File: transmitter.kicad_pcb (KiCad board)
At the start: 6 copper layers, 0 parts

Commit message: added schematics and pcb, configure project
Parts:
- added C1: 100nF, 0_capacitors:C_0402_1005Metric, F.Cu at (148.1, 165.1)
- added C10: 100nF, 0_capacitors:C_0402_1005Metric, F.Cu at (108.5, 208.5)
- added C11: 100nF, 0_capacitors:C_0402_1005Metric, F.Cu at (108.5, 210.5)
- added C12: 4.7uF, 0_capacitors:C_0805_2012Metric, F.Cu at (104.9, 209.1)
- added C13: 4.7uF, 0_capacitors:C_0805_2012Metric, F.Cu at (104.9, 212.1)
- added C2: 100nF, 0_capacitors:C_0402_1005Metric, F.Cu at (148.1, 167.1)
- added C3: 100nF, 0_capacitors:C_0402_1005Metric, F.Cu at (148.1, 169.1)
- added C4: 100nF, 0_capacitors:C_0402_1005Metric, F.Cu at (148.1, 171.0)
- added C5: 100nF, 0_capacitors:C_0402_1005Metric, F.Cu at (148.1, 173.0)
- added C6: 100nF, 0_capacitors:C_0402_1005Metric, F.Cu at (148.1, 175.0)
- added C7: 100nF, 0_capacitors:C_0402_1005Metric, F.Cu at (148.1, 176.9)
- added C8: 100nF, 0_capacitors:C_0402_1005Metric, F.Cu at (155.9, 191.8)
- added C9: 100nF, 0_capacitors:C_0402_1005Metric, F.Cu at (141.1, 193.0)
- added CARD1: ~, 0_connectors:TF-SMD_TF-PUSH, F.Cu at (160.4, 170.7)
- added IC1: W9864G6KH-6, 0_integrated_circuits:SOP80P1176X120-54N, F.Cu at (139.5, 176.1)
- added IC2: TPS61165DBVR, 0_integrated_circuits:SOT95P280X145-6N, F.Cu at (135.0, 192.3)
- added J1: AFC01-S40FCA-00, 0_connectors:AFC01S40FCA00, F.Cu at (76.8, 203.2)
- added J2: AFC07-S10ECC-00, 0_connectors:AFC07S10ECC00, F.Cu at (108.0, 202.9)
- added R1: 10kΩ, 0_resistors:R_0402_1005Metric, F.Cu at (153.0, 184.1)
- added R2: 10kΩ, 0_resistors:R_0402_1005Metric, F.Cu at (153.0, 186.0)
- added R3: 10kΩ, 0_resistors:R_0402_1005Metric, F.Cu at (153.0, 188.0)
- added R4: 10kΩ, 0_resistors:R_0402_1005Metric, F.Cu at (153.0, 190.0)
- added R5: 0Ω, 0_resistors:R_0402_1005Metric, F.Cu at (153.0, 192.0)
- added R6: 0Ω, 0_resistors:R_0402_1005Metric, F.Cu at (153.0, 194.0)
- added R7: 10kΩ, 0_resistors:R_0402_1005Metric, F.Cu at (141.1, 191.0)
- added R8: 10kΩ, 0_resistors:R_0402_1005Metric, F.Cu at (111.4, 208.5)
- added U1: STM32H743ZIT6TR, 0_integrated_circuits:LQFP-144_1_STM, F.Cu at (120.7, 151.3)
- added U2: CAT24C256, 0_integrated_circuits:SOIC-8_5.3x6.2mm_P1.27mm, F.Cu at (159.7, 186.9)
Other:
- board outline added: 200 x 200 mm
- copper layers 6 -> 2
- rule pad_to_mask_clearance: 0.05 -> 0
- board text removed: "??? ??? ???"
- board text removed: "??? ??? ??? ??? ??? (slot) ??? ??? ??? ??? ???"
- board text removed: "???mm"
- board text removed: "???mm (?oz)"
- board text removed: "???mm ???mm ???mm ???mm ???mm ???mm ???mm ???mm ???mm ???mm"
- board text removed: "ASSEMBLY NOTES (UNLESS OTHERWISE SPECIFIED) 1) DO NOT POPULATE PARTS ARE MARKED WITH A RED CROSS. 2) DO NOT POPULATE PARTS ARE NOT PRESENT IN THE BOM. 3) IF CONFLICTING INFORMATION IS FOUND BETWEEN THE ASSEMBLY FILE AND BOM, BOM SHOULD BE USED AS THE MAIN SOURCE."
- board text removed: "All dimensions are in millimeters unless otherwise specified."
- board text removed: "B.Mask"
- board text removed: "B.Paste"
- board text removed: "B.Silkscreen"
- board text removed: "Back Side"
- board text removed: "Bottom Assembly (Scale 1:1)"
- board text removed: "Bottom Fabrication (Scale 1:1)"
- board text removed: "Bottom Test Points (Scale 1:1)"
- board text removed: "Bottom View"
- board text removed: "Components"
- board text removed: "Copper"
- board text removed: "Core"
- board text removed: "Count"
- board text removed: "Dielectric"
- board text removed: "Dielectric Material"
- board text removed: "Drill Drawing (Top View) (Scale 1:1)"
- board text removed: "F.Mask"
- board text removed: "F.Paste"
- board text removed: "F.Silkscreen"
- board text removed: "FABRICATION NOTES (UNLESS OTHERWISE SPECIFIED) 1) OUTLINE DEFINED IN SEPARATE GERBER FILE WITH {dblquote}Edge_Cuts.GBR{dblquote} SUFFIX. DIMENSIONS OF CIRCUMSIZED RECTANGLE SHOWN ON THIS DWG FOR REF ONLY. 2) SEE SEPARATE DRILL FILES WITH {dblquote}.DRL{dblquote} SUFFIX FOR HOLE LOCATIONS. SELECTED HOLE LOCATIONS SHOWN ON THIS DWG FOR REF ONLY. 3) IMPEDANCE CONTROL REQUIRED. Microstrip 100-Ohm Dif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"
- board text removed: "FR-4"
- board text removed: "Front Side"
- board text removed: "GBR"
- board text removed: "Gerber"
- board text removed: "Hole Size"
- board text removed: "Internal Plane"
- board text removed: "L1 (Sig, PWR)"
- board text removed: "L2 (GND)"
- board text removed: "L3 (Sig, PWR)"
- board text removed: "L4 (Sig, PWR)"
- board text removed: "L5 (GND)"
- board text removed: "L6 (Sig, PWR)"
- board text removed: "Layer"
- board text removed: "Layer Stack Legend"
- board text removed: "Legend"
- board text removed: "Material"
- board text removed: "Net"
- board text removed: "Note: external layer thicknesses are specified after plating."
- board text removed: "PCB3D_BR_BOARDNAME"
- board text removed: "PCB3D_TL_BOARDNAME"
- board text removed: "Paste Mask"
- board text removed: "Plated"
- board text removed: "Plated Plated Plated Plated Plated Plated Plated Plated Plated Unplated"
- board text removed: "Prepreg"
- board text removed: "Ref."
- board text removed: "Signal"
- board text removed: "Solder Mask"
- board text removed: "Solder Resist"
- board text removed: "Symbol"
- board text removed: "THT SMD Total"
- board text removed: "TP? TP? TP?"
- board text removed: "Thickness"
- board text removed: "Top Assembly (Scale 1:1)"
- board text removed: "Top Fabrication (Scale 1:1)"
- board text removed: "Top Test Points (Scale 1:1)"
- board text removed: "Top View"
- board text removed: "Total"
- board text removed: "Total thickness: 1.62mm"
- board text removed: "Type"
- board text removed: "X"
- board text removed: "X [mm]"
- board text removed: "Y"
- board text removed: "Y [mm]"

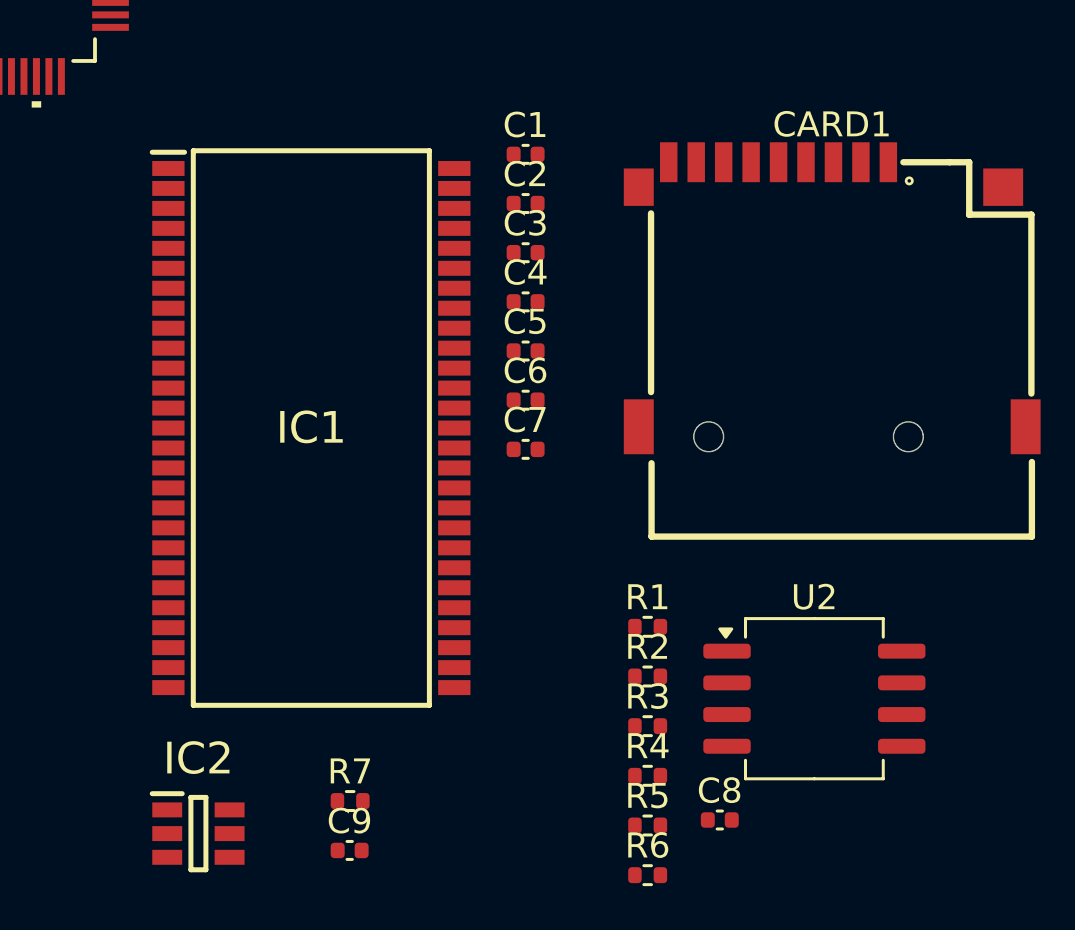
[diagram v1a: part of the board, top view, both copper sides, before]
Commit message: added lcd backlight schematic
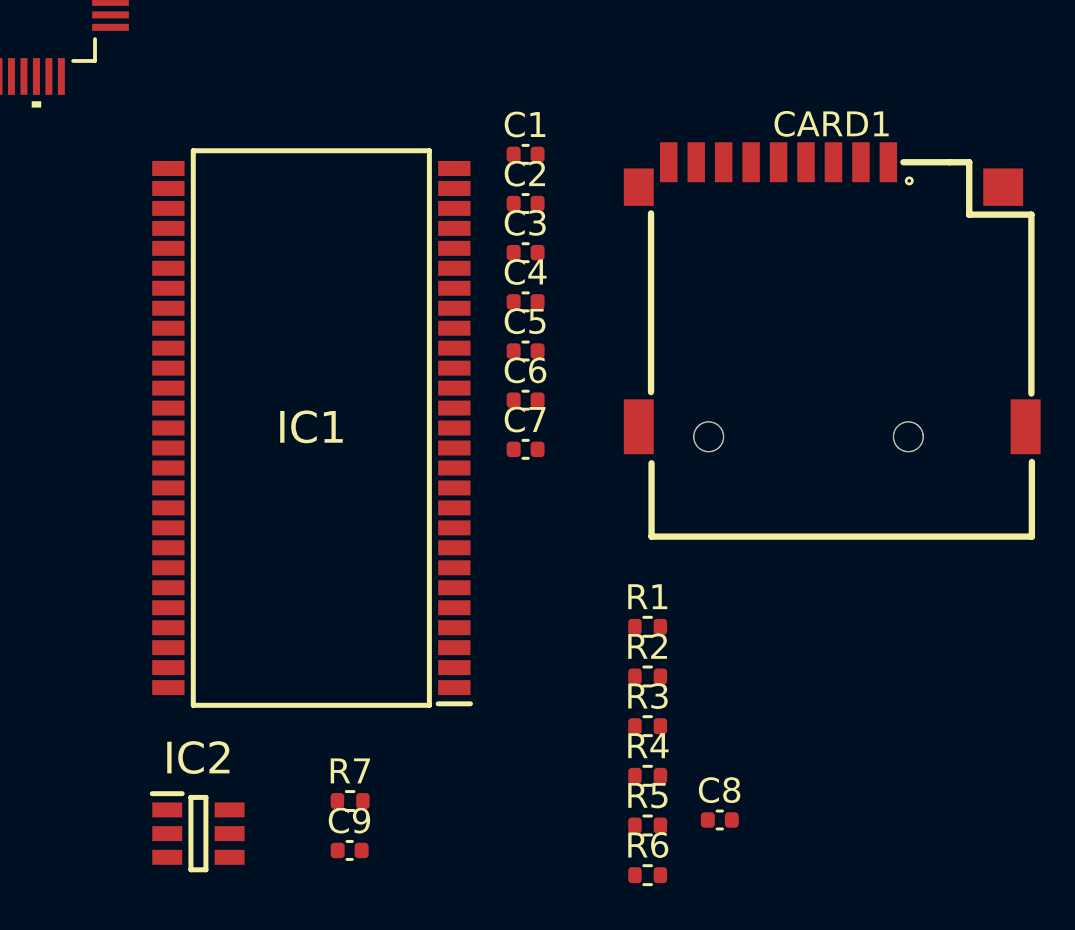
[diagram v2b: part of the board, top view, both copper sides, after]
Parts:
- removed U2: CAT24C256, 0_integrated_circuits:SOIC-8_5.3x6.2mm_P1.27mm
- turned IC1 to 180 degrees

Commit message: update project structure and import to pcb
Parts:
- added BZ1: Buzzer, Buzzer_Beeper:Buzzer_TDK_PS1240P02BT_D12.2mm_H6.5mm, F.Cu at (329.8, 83.2)
- added C14: 4.7uF, 0_capacitors:C_0805_2012Metric, F.Cu at (298.9, 29.1)
- added C15: 100nF, 0_capacitors:C_0402_1005Metric, F.Cu at (302.6, 38.7)
- added C16: 4.7uF, 0_capacitors:C_0805_2012Metric, F.Cu at (298.9, 32.1)
- added C17: 4.7uF, 0_capacitors:C_0805_2012Metric, F.Cu at (298.9, 35.1)
- added C18: 220nF, 0_capacitors:C_0402_1005Metric, F.Cu at (302.6, 40.7)
- added C19: 10uF 16V, 0_capacitors:CP_EIA-3216-18_Kemet-A, F.Cu at (252.9, 48.3)
- added C20: 100nF, 0_capacitors:C_0402_1005Metric, F.Cu at (264.5, 47.7)
- added C21: 4.7uF, 0_capacitors:C_0805_2012Metric, F.Cu at (257.9, 48.2)
- added C22: 100nF, 0_capacitors:C_0402_1005Metric, F.Cu at (148.0, 91.2)
- added C23: 100nF, 0_capacitors:C_0402_1005Metric, F.Cu at (328.6, 105.6)
- added C24: 100nF, 0_capacitors:C_0402_1005Metric, F.Cu at (328.6, 107.5)
- added C25: 100nF, 0_capacitors:C_0402_1005Metric, F.Cu at (328.6, 109.5)
- added C26: 100nF, 0_capacitors:C_0402_1005Metric, F.Cu at (328.6, 111.5)
- added C27: 100nF, 0_capacitors:C_0402_1005Metric, F.Cu at (285.8, 78.9)
- added C28: 100nF, 0_capacitors:C_0402_1005Metric, F.Cu at (285.8, 80.9)
- added C29: 100nF, 0_capacitors:C_0402_1005Metric, F.Cu at (285.8, 82.9)
- added C30: 100nF, 0_capacitors:C_0402_1005Metric, F.Cu at (285.8, 84.8)
- added C31: 100nF, 0_capacitors:C_0402_1005Metric, F.Cu at (285.8, 86.8)
- added C32: 100nF, 0_capacitors:C_0402_1005Metric, F.Cu at (285.8, 88.8)
- added C33: 100nF, 0_capacitors:C_0402_1005Metric, F.Cu at (285.8, 90.7)
- added C34: 100nF, 0_capacitors:C_0402_1005Metric, F.Cu at (285.8, 92.7)
- added C35: 100nF, 0_capacitors:C_0402_1005Metric, F.Cu at (332.4, 35.2)
- added C36: 100nF, 0_capacitors:C_0402_1005Metric, F.Cu at (332.4, 37.1)
- added C37: 4.7uF, 0_capacitors:C_0805_2012Metric, F.Cu at (334.2, 98.1)
- added C38: 100nF, 0_capacitors:C_0402_1005Metric, F.Cu at (341.8, 104.7)
- added C39: 4.7uF, 0_capacitors:C_0805_2012Metric, F.Cu at (334.2, 101.2)
- added C40: 10uF, 0_capacitors:C_0805_2012Metric, F.Cu at (333.4, 65.7)
- added C41: 100nF, 0_capacitors:C_0402_1005Metric, F.Cu at (341.8, 106.7)
- added C42: 10uF, 0_capacitors:C_0805_2012Metric, F.Cu at (334.2, 104.2)
- added C43: 100nF, 0_capacitors:C_0402_1005Metric, F.Cu at (340.0, 65.1)
- added C44: 10uF, 0_capacitors:C_0805_2012Metric, F.Cu at (293.2, 62.5)
- added C45: 10uF, 0_capacitors:C_0805_2012Metric, F.Cu at (293.2, 65.6)
- added C46: 1uF, 0_capacitors:C_0603_1608Metric, F.Cu at (279.3, 68.4)
- added C47: 100nF, 0_capacitors:C_0402_1005Metric, F.Cu at (282.8, 68.1)
- added C48: 100pF, 0_capacitors:C_0603_1608Metric, F.Cu at (279.3, 70.9)
- added C49: 22uF, 0_capacitors:C_0805_2012Metric, F.Cu at (293.2, 68.6)
- added C50: 22uF, 0_capacitors:C_0805_2012Metric, F.Cu at (293.2, 71.6)
- added C51: 10uF 16V, 0_capacitors:CP_EIA-3216-18_Kemet-A, F.Cu at (298.5, 62.6)
- added C52: 10uF 16V, 0_capacitors:CP_EIA-3216-18_Kemet-A, F.Cu at (298.5, 65.8)
- added C53: 100nF, 0_capacitors:C_0402_1005Metric, F.Cu at (282.8, 70.1)
- added C54: 100nF, 0_capacitors:C_0402_1005Metric, F.Cu at (282.8, 72.0)
- added C55: 100nF, 0_capacitors:C_0402_1005Metric, F.Cu at (251.2, 78.6)
- added C56: 100nF, 0_capacitors:C_0402_1005Metric, F.Cu at (251.2, 80.6)
- added C57: 100nF, 0_capacitors:C_0402_1005Metric, F.Cu at (251.2, 82.6)
- added C58: 100nF, 0_capacitors:C_0402_1005Metric, F.Cu at (251.2, 84.5)
- added C59: 100nF, 0_capacitors:C_0402_1005Metric, F.Cu at (251.2, 86.5)
- added C60: 100nF, 0_capacitors:C_0402_1005Metric, F.Cu at (251.2, 88.5)
- added C61: 100nF, 0_capacitors:C_0402_1005Metric, F.Cu at (254.1, 78.6)
- added C62: 100nF, 0_capacitors:C_0402_1005Metric, F.Cu at (254.1, 80.6)
- added C63: 100nF, 0_capacitors:C_0402_1005Metric, F.Cu at (254.1, 82.6)
- added C64: 100nF, 0_capacitors:C_0402_1005Metric, F.Cu at (254.1, 84.5)
- added C65: 100nF, 0_capacitors:C_0402_1005Metric, F.Cu at (254.1, 86.5)
- added C66: 1uF, 0_capacitors:C_0603_1608Metric, F.Cu at (270.4, 85.5)
- added C67: 1uF, 0_capacitors:C_0603_1608Metric, F.Cu at (270.4, 88.0)
- added C68: 1uF, 0_capacitors:C_0603_1608Metric, F.Cu at (270.4, 90.5)
- added C69: 100nF, 0_capacitors:C_0402_1005Metric, F.Cu at (254.1, 88.5)
- added C70: 100nF, 0_capacitors:C_0402_1005Metric, F.Cu at (256.9, 78.6)
- added C71: 4.7uF, 0_capacitors:C_0805_2012Metric, F.Cu at (272.9, 79.2)
- added C72: 2.2uF, 0_capacitors:C_1206_3216Metric, F.Cu at (265.6, 85.9)
- added C73: 2.2uF, 0_capacitors:C_1206_3216Metric, F.Cu at (265.6, 89.2)
- added C74: 100nF, 0_capacitors:C_0402_1005Metric, F.Cu at (256.9, 80.6)
- added C75: 100nF, 0_capacitors:C_0402_1005Metric, F.Cu at (256.9, 82.6)
- added C76: 100nF, 0_capacitors:C_0402_1005Metric, F.Cu at (281.6, 114.2)
- added C77: 100nF, 0_capacitors:C_0402_1005Metric, F.Cu at (281.6, 116.1)
- added C78: 100nF, 0_capacitors:C_0402_1005Metric, F.Cu at (281.6, 118.1)
- added C79: 100nF, 0_capacitors:C_0402_1005Metric, F.Cu at (258.4, 101.4)
- added C80: 100nF, 0_capacitors:C_0402_1005Metric, F.Cu at (258.4, 103.3)
- added C81: 6.8pF, 0_capacitors:C_0402_1005Metric, F.Cu at (258.4, 105.3)
- added C82: 6.8pF, 0_capacitors:C_0402_1005Metric, F.Cu at (258.4, 107.3)
- added C83: 6.8pF, 0_capacitors:C_0402_1005Metric, F.Cu at (258.4, 109.3)
- added C84: 6.8pF, 0_capacitors:C_0402_1005Metric, F.Cu at (258.4, 111.2)
- added C85: 1uF, 0_capacitors:C_0603_1608Metric, F.Cu at (271.1, 109.6)
- added D1: 1N5819WS, 0_diodes:D_SOD-323, F.Cu at (308.6, 39.6)
- added D2: 1N5819WS, 0_diodes:D_SOD-323, F.Cu at (339.7, 79.4)
- added D3: 1N5819WS, 0_diodes:D_SOD-323, F.Cu at (297.6, 74.5)
- added D4: RED, LED_SMD:LED_0603_1608Metric, F.Cu at (314.8, 42.9)
- added D5: WHITE, LED_SMD:LED_0603_1608Metric, F.Cu at (314.8, 45.5)
- added E01-2G4M27D1: DS1023-2*4SF11, 0_modules:PE01-ML01DP5, F.Cu at (121.9, 39.2)
- added IC3: MT25QL128ABA1ESE-0SIT, 0_integrated_circuits:SOIC127P790X216-8L, F.Cu at (148.5, 86.9)
- added IC4: USBLC6-2SC6, 0_integrated_circuits:SOT95P280X145-6N, F.Cu at (328.6, 66.4)
- added J10: ~, Connector_PinHeader_2.54mm:PinHeader_1x02_P2.54mm_Vertical, F.Cu at (266.7, 117.2)
- added J3: B2B-PH-K-S, Connector_JST:JST_PH_B2B-PH-K_1x02_P2.00mm_Vertical, F.Cu at (265.7, 80.4)
- added J4: B2B-PH-K-S, Connector_JST:JST_PH_B2B-PH-K_1x02_P2.00mm_Vertical, F.Cu at (335.0, 119.5)
- added J5: B3B-PH-K-S, Connector_JST:JST_PH_B3B-PH-K_1x03_P2.00mm_Vertical, F.Cu at (335.0, 112.9)
- added J6: USB4085-GF-A, 0_connectors:GCT_USB4085-GF-A_REVB, F.Cu at (49.4, 25.9)
- added J7: Conn_01x05, Connector_JST:JST_PH_B5B-PH-K_1x05_P2.00mm_Vertical, F.Cu at (259.9, 96.6)
- added J8: ~, Connector_PinHeader_2.54mm:PinHeader_1x02_P2.54mm_Vertical, F.Cu at (262.1, 117.2)
- added J9: Conn_02x06_Odd_Even, Connector_PinSocket_2.54mm:PinSocket_2x06_P2.54mm_Vertical, F.Cu at (254.6, 96.2)
- added JP1: NO, Jumper:SolderJumper-2_P1.3mm_Open_TrianglePad1.0x1.5mm, F.Cu at (298.1, 58.2)
- added JP10: NO, Jumper:SolderJumper-2_P1.3mm_Open_TrianglePad1.0x1.5mm, F.Cu at (338.6, 102.0)
- added JP2: NC, Jumper:SolderJumper-2_P1.3mm_Open_TrianglePad1.0x1.5mm, F.Cu at (260.6, 79.4)
- added JP3: NO, Jumper:SolderJumper-2_P1.3mm_Open_TrianglePad1.0x1.5mm, F.Cu at (260.6, 83.0)
- added JP4: NC, Jumper:SolderJumper-2_P1.3mm_Open_TrianglePad1.0x1.5mm, F.Cu at (271.1, 116.7)
- added JP5: NC, Jumper:SolderJumper-2_P1.3mm_Open_TrianglePad1.0x1.5mm, F.Cu at (260.6, 86.5)
- added JP6: NC, Jumper:SolderJumper-2_P1.3mm_Open_TrianglePad1.0x1.5mm, F.Cu at (260.6, 90.1)
- added JP7: SolderJumper_3_Bridged12, Jumper:SolderJumper-3_P2.0mm_Open_TrianglePad1.0x1.5mm_NumberLabels, F.Cu at (330.5, 90.3)
- added JP8: NO, Jumper:SolderJumper-2_P1.3mm_Open_TrianglePad1.0x1.5mm, F.Cu at (271.1, 120.2)
- added JP9: NO, Jumper:SolderJumper-2_P1.3mm_Open_TrianglePad1.0x1.5mm, F.Cu at (338.6, 98.4)
- added L1: 1.33A 10uH, 0_inductors:IND_VLS3012HBX-100M, F.Cu at (308.0, 30.1)
- added L2: GZ2012D601TF, 0_inductors:L_0805_2012Metric, F.Cu at (303.4, 29.0)
- added L3: GZ2012D601TF, 0_inductors:L_0805_2012Metric, F.Cu at (303.4, 31.8)
- added L4: 1.8A 1uH, Inductor_SMD:L_Cenker_CKCS4018, F.Cu at (298.4, 70.2)
- added Q1: AO3400A, Package_TO_SOT_SMD:SOT-23, F.Cu at (288.5, 63.4)
- added Q2: AO3400A, Package_TO_SOT_SMD:SOT-23, F.Cu at (288.5, 68.1)
- added Q3: SI2301CDS-T1-GE3, 0_transistors:SOT-23, F.Cu at (288.5, 72.7)
- added Q4: AO3400A, Package_TO_SOT_SMD:SOT-23, F.Cu at (336.5, 90.9)
- added R10: 10kΩ, 0_resistors:R_0402_1005Metric, F.Cu at (298.2, 39.6)
- added R11: 1Ω, 0_resistors:R_0603_1608Metric, F.Cu at (308.4, 34.4)
- added R12: 2Ω, 0_resistors:R_0603_1608Metric, F.Cu at (308.4, 36.9)
- added R13: 10kΩ, 0_resistors:R_0402_1005Metric, F.Cu at (261.6, 47.7)
- added R14: 10kΩ, 0_resistors:R_0402_1005Metric, F.Cu at (261.6, 49.7)
- added R15: 10kΩ, 0_resistors:R_0402_1005Metric, F.Cu at (145.1, 91.2)
- added R16: 0Ω, 0_resistors:R_0402_1005Metric, F.Cu at (328.6, 97.6)
- added R17: 0Ω, 0_resistors:R_0402_1005Metric, F.Cu at (328.6, 99.6)
- added R18: 0Ω, 0_resistors:R_0402_1005Metric, F.Cu at (328.6, 101.6)
- added R19: 0Ω, 0_resistors:R_0402_1005Metric, F.Cu at (328.6, 103.6)
- added R20: 47kΩ, 0_resistors:R_0402_1005Metric, F.Cu at (285.8, 94.7)
- added R21: 5.1kΩ, 0_resistors:R_0402_1005Metric, F.Cu at (285.8, 96.7)
- added R22: 5.1kΩ, 0_resistors:R_0402_1005Metric, F.Cu at (285.8, 98.7)
- added R23: 47kΩ, 0_resistors:R_0402_1005Metric, F.Cu at (285.8, 100.7)
- added R24: 5.1kΩ, 0_resistors:R_0402_1005Metric, F.Cu at (288.7, 94.7)
- added R25: 47kΩ, 0_resistors:R_0402_1005Metric, F.Cu at (288.7, 96.7)
- added R26: 5.1kΩ, 0_resistors:R_0402_1005Metric, F.Cu at (288.7, 98.7)
- added R27: 47kΩ, 0_resistors:R_0402_1005Metric, F.Cu at (288.7, 100.7)
- added R28: 5.1kΩ, 0_resistors:R_0402_1005Metric, F.Cu at (291.6, 94.7)
- added R29: 47kΩ, 0_resistors:R_0402_1005Metric, F.Cu at (291.6, 96.7)
- added R30: 5.1kΩ, 0_resistors:R_0402_1005Metric, F.Cu at (291.6, 98.7)
- added R31: 47kΩ, 0_resistors:R_0402_1005Metric, F.Cu at (291.6, 100.7)
- added R32: 5.1kΩ, 0_resistors:R_0402_1005Metric, F.Cu at (294.5, 94.7)
- added R33: 47kΩ, 0_resistors:R_0402_1005Metric, F.Cu at (294.5, 96.7)
- added R34: 5.1kΩ, 0_resistors:R_0402_1005Metric, F.Cu at (294.5, 98.7)
- added R35: 47kΩ, 0_resistors:R_0402_1005Metric, F.Cu at (294.5, 100.7)
- added R36: 5.1kΩ, 0_resistors:R_0402_1005Metric, F.Cu at (329.5, 28.6)
- added R37: 47kΩ, 0_resistors:R_0402_1005Metric, F.Cu at (329.5, 30.6)
- added R38: 5.1kΩ, 0_resistors:R_0402_1005Metric, F.Cu at (329.5, 32.6)
- added R39: 47kΩ, 0_resistors:R_0402_1005Metric, F.Cu at (329.5, 34.6)
- added R40: 47kΩ, 0_resistors:R_0402_1005Metric, F.Cu at (322.5, 53.7)
- added R41: 47kΩ, 0_resistors:R_0402_1005Metric, F.Cu at (322.5, 55.7)
- added R42: 47kΩ, 0_resistors:R_0402_1005Metric, F.Cu at (322.5, 57.7)
- added R43: 47kΩ, 0_resistors:R_0402_1005Metric, F.Cu at (322.5, 59.7)
- added R44: 47kΩ, 0_resistors:R_0402_1005Metric, F.Cu at (322.5, 61.7)
- added R45: 0Ω, 0_resistors:R_0402_1005Metric, F.Cu at (322.5, 63.7)
- added R46: 47kΩ, 0_resistors:R_0402_1005Metric, F.Cu at (322.5, 65.7)
- added R47: 10kΩ, 0_resistors:R_0402_1005Metric, F.Cu at (342.3, 97.6)
- added R48: 10kΩ, 0_resistors:R_0402_1005Metric, F.Cu at (342.3, 99.6)
- added R49: 300kΩ, 0_resistors:R_0603_1608Metric, F.Cu at (334.0, 106.9)
- added R50: 0Ω, 0_resistors:R_0402_1005Metric, F.Cu at (342.3, 101.6)
- added R51: 5.1kΩ, 0_resistors:R_0402_1005Metric, F.Cu at (337.1, 65.1)
- added R52: 5.1kΩ, 0_resistors:R_0402_1005Metric, F.Cu at (337.1, 67.1)
- added R53: 100kΩ, 0_resistors:R_0402_1005Metric, F.Cu at (278.8, 53.7)
- added R54: 0Ω, 0_resistors:R_0402_1005Metric, F.Cu at (278.8, 55.7)
- added R55: 0Ω, 0_resistors:R_0402_1005Metric, F.Cu at (278.8, 57.7)
- added R56: 47kΩ, 0_resistors:R_0402_1005Metric, F.Cu at (278.8, 59.7)
- added R57: 10kΩ, 0_resistors:R_0402_1005Metric, F.Cu at (278.8, 61.7)
- added R58: 0Ω, 0_resistors:R_0402_1005Metric, F.Cu at (281.7, 53.7)
- added R59: 0Ω, 0_resistors:R_0402_1005Metric, F.Cu at (281.7, 55.7)
- added R60: 100kΩ, 0_resistors:R_0402_1005Metric, F.Cu at (281.7, 57.7)
- added R61: 0Ω, 0_resistors:R_0402_1005Metric, F.Cu at (273.9, 85.2)
- added R62: 100kΩ, 0_resistors:R_0402_1005Metric, F.Cu at (281.7, 59.7)
- added R63: 330Ω, 0_resistors:R_0402_1005Metric, F.Cu at (281.7, 61.7)
- added R64: 300kΩ, 0_resistors:R_0603_1608Metric, F.Cu at (279.3, 73.4)
- added R65: 1kΩ, 0_resistors:R_0402_1005Metric, F.Cu at (284.6, 53.7)
- added R66: 100kΩ, 0_resistors:R_0402_1005Metric, F.Cu at (284.6, 55.7)
- added R67: 634kΩ, 0_resistors:R_0402_1005Metric, F.Cu at (284.6, 57.7)
- added R68: 0Ω, 0_resistors:R_0402_1005Metric, F.Cu at (273.9, 87.2)
- added R69: 10kΩ, 0_resistors:R_0402_1005Metric, F.Cu at (278.8, 107.6)
- added R70: 10kΩ, 0_resistors:R_0402_1005Metric, F.Cu at (278.8, 109.6)
- added R71: 10kΩ, 0_resistors:R_0402_1005Metric, F.Cu at (278.8, 111.6)
- added R72: 10kΩ, 0_resistors:R_0402_1005Metric, F.Cu at (278.8, 113.6)
- added R73: 5.1kΩ, 0_resistors:R_0402_1005Metric, F.Cu at (278.8, 115.6)
- added R74: 47kΩ, 0_resistors:R_0402_1005Metric, F.Cu at (278.8, 117.6)
- added R75: 330Ω, 0_resistors:R_0402_1005Metric, F.Cu at (339.0, 81.9)
- added R76: 47kΩ, 0_resistors:R_0402_1005Metric, F.Cu at (339.0, 83.9)
- added R77: 1kΩ, 0_resistors:R_0402_1005Metric, F.Cu at (318.2, 42.6)
- added R78: 1kΩ, 0_resistors:R_0402_1005Metric, F.Cu at (318.2, 44.5)
- added R79: 10kΩ, 0_resistors:R_0402_1005Metric, F.Cu at (261.2, 101.4)
- added R80: 0Ω, 0_resistors:R_0402_1005Metric, F.Cu at (261.2, 103.4)
- added R81: 0Ω, 0_resistors:R_0402_1005Metric, F.Cu at (261.2, 105.4)
- added R82: 0Ω, 0_resistors:R_0402_1005Metric, F.Cu at (261.2, 107.4)
- added R83: 0Ω, 0_resistors:R_0402_1005Metric, F.Cu at (264.2, 101.4)
- added R84: 10kΩ, 0_resistors:R_0402_1005Metric, F.Cu at (264.2, 103.4)
- added R85: 10kΩ, 0_resistors:R_0402_1005Metric, F.Cu at (264.2, 105.4)
- added R86: 10kΩ, 0_resistors:R_0402_1005Metric, F.Cu at (264.2, 107.4)
- added R87: 0Ω, 0_resistors:R_0402_1005Metric, F.Cu at (267.1, 101.4)
- added R88: 0Ω, 0_resistors:R_0402_1005Metric, F.Cu at (267.1, 103.4)
- added R89: 5.1kΩ, 0_resistors:R_0402_1005Metric, F.Cu at (267.1, 105.4)
- added R9: 0Ω, 0_resistors:R_0402_1005Metric, F.Cu at (298.2, 37.6)
- added R90: 5.1kΩ, 0_resistors:R_0402_1005Metric, F.Cu at (267.1, 107.4)
- added R91: 10kΩ, 0_resistors:R_0402_1005Metric, F.Cu at (270.0, 101.4)
- added R92: 10kΩ, 0_resistors:R_0402_1005Metric, F.Cu at (270.0, 103.4)
- added R93: 10kΩ, 0_resistors:R_0402_1005Metric, F.Cu at (270.0, 105.4)
- added R94: 10kΩ, 0_resistors:R_0402_1005Metric, F.Cu at (270.0, 107.4)
- added RV1: LeftX, 0_connectors:JST_PH_B3B-PH-K_1x03_P2.00mm_Vertical, F.Cu at (320.1, 99.4)
- added RV2: LeftY, 0_connectors:JST_PH_B3B-PH-K_1x03_P2.00mm_Vertical, F.Cu at (320.1, 105.9)
- added RV3: RightX, 0_connectors:JST_PH_B3B-PH-K_1x03_P2.00mm_Vertical, F.Cu at (320.1, 112.5)
- added RV4: RightY, 0_connectors:JST_PH_B3B-PH-K_1x03_P2.00mm_Vertical, F.Cu at (320.1, 119.0)
- added S1: SKRTLAE010, 0_switches:SKRTLAE010, F.Cu at (291.4, 81.6)
- added S2: SKRTLAE010, 0_switches:SKRTLAE010, F.Cu at (291.4, 88.6)
- added SW1: Button SPST SMD Tactile Switch, 0_switches:SW_TS-1088-AR02016, F.Cu at (280.8, 80.2)
- added SW2: Button SPST SMD Tactile Switch, 0_switches:SW_TS-1088-AR02016, F.Cu at (280.8, 84.6)
- added SW3: Button SPST SMD Tactile Switch, 0_switches:SW_TS-1088-AR02016, F.Cu at (280.8, 89.1)
- added SW4: Button SPST SMD Tactile Switch, 0_switches:SW_TS-1088-AR02016, F.Cu at (280.8, 93.5)
- added SW5: Button SPST SMD Tactile Switch, 0_switches:SW_TS-1088-AR02016, F.Cu at (280.8, 98.0)
- added SW6: Button SPST SMD Tactile Switch, 0_switches:SW_TS-1088-AR02016, F.Cu at (280.8, 102.4)
- added SW7: SW_SPDT_MSM, 0_connectors:JST_PH_B3B-PH-K_1x03_P2.00mm_Vertical, F.Cu at (333.9, 30.4)
- added SW8: Button SPST SMD Tactile Switch, 0_switches:SW_TS-1088-AR02016, F.Cu at (280.8, 64.9)
- added SW9: RotaryEncoder_Switch, Connector_JST:JST_PH_B5B-PH-K_1x05_P2.00mm_Vertical, F.Cu at (283.2, 109.4)
- added U2: CAT24C256, 0_integrated_circuits:SOIC-8_5.3x6.2mm_P1.27mm, F.Cu at (320.8, 31.5)
- added U3: MP2667GG-0000-Z, 0_integrated_circuits:QFN-10_2MMx2MM_MNP-L, F.Cu at (338.4, 106.0)
- added U4: AMS1117-3.3, Package_TO_SOT_SMD:SOT-223-3_TabPin2, F.Cu at (291.0, 56.9)
- added U5: TPS61252DSG, Package_SON:WSON-8-1EP_2x2mm_P0.5mm_EP0.9x1.6mm, F.Cu at (298.1, 54.6)
- added U6: PCA9554APW, 0_integrated_circuits:SOP65P640X120-16N, F.Cu at (264.7, 111.6)
- added Y1: 32.768KHZ, 0_oscillators:X322525MOB4SI 25MHz, F.Cu at (136.9, 69.9)
- added Y2: X322525MOB4SI-25MHz, 0_oscillators:X322525MOB4SI 25MHz, F.Cu at (136.9, 74.4)
- moved C12 240.6 mm to (312.9, 88.2)
- moved C13 240.6 mm to (312.9, 91.2)
- moved C10 239.6 mm to (316.5, 89.6)
- moved C11 239.6 mm to (316.5, 91.6)
- moved R8 239.6 mm to (319.4, 89.7)
- moved IC2 230.5 mm to (303.8, 35.4)
- moved C8 223.9 mm to (317.1, 36.4)
- moved R1 223.9 mm to (314.2, 28.6)
- moved R2 223.9 mm to (314.2, 30.6)
- moved R3 223.9 mm to (314.2, 32.6)
- moved R4 223.9 mm to (314.2, 34.6)
- moved R5 223.9 mm to (314.2, 36.6)
- moved R6 223.9 mm to (314.2, 38.6)
- moved R7 206.1 mm to (319.4, 87.7)
- moved C9 204.7 mm to (316.5, 87.7)
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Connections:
- net /Project Architecture/LCD - Connectors/CTP_INTERRUPT renamed /Project Architecture/LCD - Connectors/CTP_IRQ
- CARD1 pad 1: unconnected-(CARD1-DAT2-Pad1) -> /Project Architecture/MCU - IO/SDMMC2_D2
- CARD1 pad 2: unconnected-(CARD1-CD/DAT3-Pad2) -> /Project Architecture/MCU - IO/SDMMC2_D3
- CARD1 pad 3: unconnected-(CARD1-CMD-Pad3) -> /Project Architecture/MCU - IO/SDMMC2_CMD
- CARD1 pad 4: unconnected-(CARD1-VDD-Pad4) -> +3.3V
- CARD1 pad 5: unconnected-(CARD1-CLX-Pad5) -> /Project Architecture/MCU - IO/SDMMC2_CK
- CARD1 pad 6: unconnected-(CARD1-VSS-Pad6) -> GND
- CARD1 pad 7: unconnected-(CARD1-DAT0-Pad7) -> /Project Architecture/MCU - IO/SDMMC2_CK
- CARD1 pad 8: unconnected-(CARD1-DAT1-Pad8) -> /Project Architecture/MCU - IO/SDMMC2_D1
- CARD1 pad CD: unconnected-(CARD1-PadCD) -> Net-(CARD1-PadCD)
- IC2 pad 1: unconnected-(IC2-VIN-Pad1) -> BLVDD
- IC2 pad 2: unconnected-(IC2-CTRL-Pad2) -> /Project Architecture/LCD - Backlight/CTRL
- IC2 pad 3: unconnected-(IC2-SW-Pad3) -> /Project Architecture/LCD - Backlight/BLHV
- IC2 pad 4: unconnected-(IC2-GND-Pad4) -> BLGND
- IC2 pad 5: unconnected-(IC2-COMP-Pad5) -> Net-(IC2-COMP)
- IC2 pad 6: unconnected-(IC2-FB-Pad6) -> /Project Architecture/LCD - Backlight/LCD_BACKLIGHT_V-
- U1 pad 103: /Project Architecture/MCU - IO/USB_OTG_FS_DM -> /Project Architecture/Interface - USB FS/USB_OTG_FS_DM
- U1 pad 104: /Project Architecture/MCU - IO/USB_OTG_FS_DP -> /Project Architecture/Interface - USB FS/USB_OTG_FS_DP
- U1 pad 105: /Project Architecture/MCU - IO/DEBUG_SWDIO -> /Project Architecture/Auxiliary/DEBUG_SWDIO
- U1 pad 106: unconnected-(U1C-VCAP-Pad106) -> VCAP
- U1 pad 107: unconnected-(U1C-VSS-Pad107) -> GND
- U1 pad 108: unconnected-(U1C-VDD-Pad108) -> +3.3V
- U1 pad 109: /Project Architecture/MCU - IO/DEBUG_SWCLK -> /Project Architecture/Auxiliary/DEBUG_SWCLK
- U1 pad 112: unconnected-(U1A-PC11-Pad112) -> /Project Architecture/MCU - IO/uC_PWR
- U1 pad 113: unconnected-(U1A-PC12-Pad113) -> /Project Architecture/MCU - IO/LED
- U1 pad 116: unconnected-(U1A-PD2-Pad116) -> /Project Architecture/MCU - IO/ENC_BUTTON
- U1 pad 118: unconnected-(U1A-PD4-Pad118) -> /Project Architecture/MCU - IO/EXPANDER_INT
- U1 pad 119: unconnected-(U1A-PD5-Pad119) -> /Project Architecture/Auxiliary/PD5
- U1 pad 120: unconnected-(U1C-VSS-Pad120) -> GND
- U1 pad 121: unconnected-(U1C-VDD-Pad121) -> +3.3V
- U1 pad 124: unconnected-(U1B-PG9-Pad124) -> /Project Architecture/Auxiliary/PG9
- U1 pad 129: unconnected-(U1B-PG14-Pad129) -> /Project Architecture/Interface - RF Transmitter/RF_CE
- U1 pad 130: unconnected-(U1C-VSS-Pad130) -> GND
- U1 pad 131: unconnected-(U1C-VDD-Pad131) -> +3.3V
- U1 pad 135: unconnected-(U1A-PB5-Pad135) -> /Project Architecture/Auxiliary/TOGGLE0
- U1 pad 137: unconnected-(U1A-PB7-Pad137) -> /Project Architecture/LCD - Backlight/BACKLIGHT_PWM
- U1 pad 138: unconnected-(U1B-BOOT0-Pad138) -> /Project Architecture/MCU - IO/BOOT0
- U1 pad 143: unconnected-(U1B-PDR_ON-Pad143) -> /Project Architecture/MCU - IO/PDR_ON
- U1 pad 144: unconnected-(U1C-VDD-Pad144) -> +3.3V
- U1 pad 16: unconnected-(U1C-VSS-Pad16) -> GND
- U1 pad 17: unconnected-(U1C-VDD-Pad17) -> +3.3V
- U1 pad 18: /Project Architecture/MCU - IO/SPI5_NSS -> /Project Architecture/Interface - RF Transmitter/SPI5_NSS
- U1 pad 19: /Project Architecture/MCU - IO/SPI5_SCK -> /Project Architecture/Interface - RF Transmitter/SPI5_SCK
- U1 pad 2: unconnected-(U1B-PE3-Pad2) -> /Project Architecture/Auxiliary/PE3
- U1 pad 20: /Project Architecture/MCU - IO/SPI5_MISO -> /Project Architecture/Interface - RF Transmitter/SPI5_MISO
- U1 pad 21: /Project Architecture/MCU - IO/SPI5_MOSI -> /Project Architecture/Interface - RF Transmitter/SPI5_MOSI
- U1 pad 23: /Project Architecture/MCU - IO/RCC_OSC_IN -> /Project Architecture/Auxiliary/RCC_OSC_IN
- U1 pad 24: /Project Architecture/MCU - IO/RCC_OSC_OUT -> /Project Architecture/Auxiliary/RCC_OSC_OUT
- U1 pad 25: unconnected-(U1B-NRST-Pad25) -> /Project Architecture/CTP_RESET
- U1 pad 30: unconnected-(U1C-VDD-Pad30) -> +3.3V
- U1 pad 31: unconnected-(U1C-VSSA-Pad31) -> GNDA
- U1 pad 32: unconnected-(U1C-VREF+-Pad32) -> VREF
- U1 pad 33: unconnected-(U1C-VDDA-Pad33) -> VDDA
- U1 pad 38: unconnected-(U1C-VSS-Pad38) -> GND
- U1 pad 39: unconnected-(U1C-VDD-Pad39) -> +3.3V
- U1 pad 51: unconnected-(U1C-VSS-Pad51) -> GND
- U1 pad 52: unconnected-(U1C-VDD-Pad52) -> +3.3V
- U1 pad 6: unconnected-(U1C-VBAT-Pad6) -> VBAT
- U1 pad 61: unconnected-(U1C-VSS-Pad61) -> GND
- U1 pad 62: unconnected-(U1C-VDD-Pad62) -> +3.3V
- U1 pad 7: unconnected-(U1A-PC13-Pad7) -> /Project Architecture/MCU - IO/BUZZER
- U1 pad 71: unconnected-(U1C-VCAP-Pad71) -> VCAP
- U1 pad 72: unconnected-(U1C-VDD-Pad72) -> +3.3V
- U1 pad 73: unconnected-(U1A-PB12-Pad73) -> /Project Architecture/Auxiliary/TOGGLE1
- U1 pad 74: unconnected-(U1A-PB13-Pad74) -> /Project Architecture/Auxiliary/PB13
- U1 pad 75: /Project Architecture/MCU - IO/SDMMC2_D0 -> /Project Architecture/MCU - IO/SDMMC2_CK
- U1 pad 8: unconnected-(U1A-PC14-OSC32_IN-Pad8) -> /Project Architecture/Auxiliary/RCC_OSC32_IN
- U1 pad 83: unconnected-(U1C-VSS-Pad83) -> GND
- U1 pad 84: unconnected-(U1C-VDD-Pad84) -> +3.3V
- U1 pad 87: unconnected-(U1B-PG2-Pad87) -> /Project Architecture/Auxiliary/PG2
- U1 pad 88: unconnected-(U1B-PG3-Pad88) -> /Project Architecture/Auxiliary/PG3
- U1 pad 9: unconnected-(U1A-PC15-OSC32_OUT-Pad9) -> /Project Architecture/Auxiliary/RCC_OSC32_OUT
- U1 pad 94: unconnected-(U1C-VSS-Pad94) -> GND
- U1 pad 95: unconnected-(U1C-VDD33USB-Pad95) -> Net-(JP5-A)
- U1 pad 98: unconnected-(U1A-PC8-Pad98) -> /Project Architecture/MCU - IO/CHARGER_INT

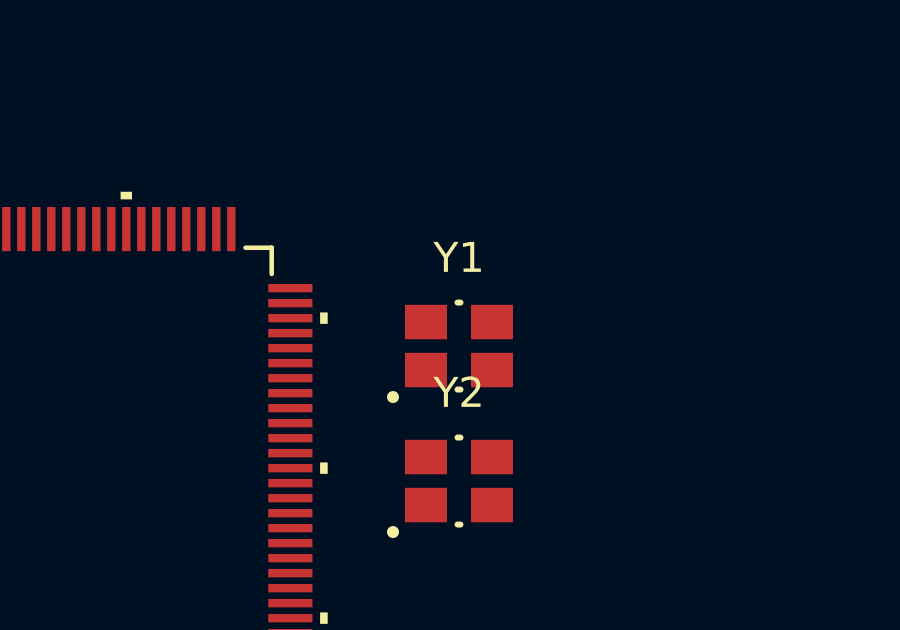
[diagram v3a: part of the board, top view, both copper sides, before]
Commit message: change 32.768kHz footrpint
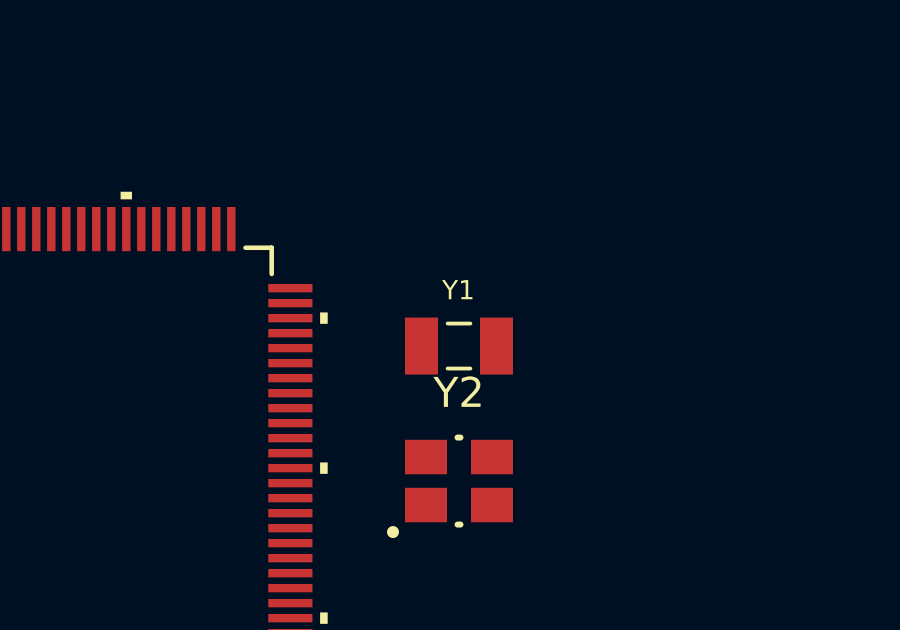
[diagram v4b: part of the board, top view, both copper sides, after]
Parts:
- Y1: footprint 0_oscillators:X322525MOB4SI 25MHz -> 0_oscillators:Q13FC13500004-32.768KHZ-4-T
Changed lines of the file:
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@@
 		(fp_text user "*"
 			(at -12.0904 -9.381 90)
+			(unlocked yes)
 			(layer "F.SilkS")
 			(effects
@@
 		(fp_text user "*"
 			(at -12.0904 -9.381 90)
-			(unlocked yes)
 			(layer "F.SilkS")
 			(effects
@@
 			)
 		)
-		(fp_text user "*"
-			(at -12.0904 -9.381 90)
+		(fp_text user "${REFERENCE}"
+			(at 0 0 90)
+			(unlocked yes)
 			(layer "F.Fab")
 			(effects
@@
 			)
 		)
-		(fp_text user "${REFERENCE}"
-			(at 0 0 90)
-			(unlocked yes)
+		(fp_text user "*"
+			(at -12.0904 -9.381 90)
 			(layer "F.Fab")
 			(effects
@@
 		)
 	)
-	(footprint "0_oscillators:X322525MOB4SI 25MHz"
+	(footprint "0_oscillators:Q13FC13500004-32.768KHZ-4-T"
 		(layer "F.Cu")
 		(at 136.9 69.9)
-		(descr "SMD3225-4P")
 		(property "Reference" "Y1"
-			(at 0 -2.935 0)
+			(at -0.018 -1.8564 0)
 			(layer "F.SilkS")
 			(effects
 				(font
-					(size 1 1)
+					(size 0.64 0.64)
 					(thickness 0.15)
 				)
@@
 		)
 		(property "Value" "32.768KHZ"
-			(at 6.76 2.965 0)
+			(at 7.7036 1.8564 0)
 			(layer "F.Fab")
 			(effects
 				(font
-					(size 1 1)
+					(size 0.64 0.64)
 					(thickness 0.15)
 				)
@@
 		(attr smd)
 		(fp_line
-			(start -0.05 -1.45)
-			(end 0.05 -1.45)
+			(start -0.38 -0.75)
+			(end 0.38 -0.75)
 			(stroke
-				(width 0.2)
+				(width 0.127)
 				(type solid)
 			)
@@
 		)
 		(fp_line
-			(start -0.05 1.45)
-			(end 0.05 1.45)
+			(start -0.38 0.75)
+			(end 0.38 0.75)
 			(stroke
-				(width 0.2)
+				(width 0.127)
 				(type solid)
 			)
 			(layer "F.SilkS")
 		)
-		(fp_circle
-			(center -2.2 1.7)
-			(end -2.1 1.7)
+		(fp_line
+			(start -2.05 -1.2)
+			(end -2.05 1.2)
 			(stroke
-				(width 0.2)
+				(width 0.05)
 				(type solid)
 			)
-			(fill no)
-			(layer "F.SilkS")
+			(layer "F.CrtYd")
 		)
-		(fp_poly
-			(pts
-				(xy -2 -1.55) (xy 2 -1.55) (xy 2 1.55) (xy -2 1.55)
+		(fp_line
+			(start -2.05 1.2)
+			(end 2.05 1.2)
+			(stroke
+				(width 0.05)
+				(type solid)
 			)
+			(layer "F.CrtYd")
+		)
+		(fp_line
+			(start 2.05 -1.2)
+			(end -2.05 -1.2)
 			(stroke
-				(width 0.1)
+				(width 0.05)
 				(type solid)
 			)
-			(fill yes)
 			(layer "F.CrtYd")
 		)
 		(fp_line
-			(start -1.7 -1.35)
-			(end 1.7 -1.35)
+			(start 2.05 1.2)
+			(end 2.05 -1.2)
 			(stroke
-				(width 0.1)
+				(width 0.05)
+				(type solid)
+			)
+			(layer "F.CrtYd")
+		)
+		(fp_line
+			(start -1.6 -0.75)
+			(end -1.6 0.75)
+			(stroke
+				(width 0.127)
 				(type solid)
 			)
@@
 		)
 		(fp_line
-			(start -1.7 1.35)
-			(end -1.7 -1.35)
+			(start -1.6 -0.75)
+			(end 1.6 -0.75)
 			(stroke
-				(width 0.1)
+				(width 0.127)
 				(type solid)
 			)
@@
 		)
 		(fp_line
-			(start 1.7 -1.35)
-			(end 1.7 1.35)
+			(start -1.6 0.75)
+			(end 1.6 0.75)
 			(stroke
-				(width 0.1)
+				(width 0.127)
 				(type solid)
 			)
@@
 		)
 		(fp_line
-			(start 1.7 1.35)
-			(end -1.7 1.35)
+			(start 1.6 -0.75)
+			(end 1.6 0.75)
 			(stroke
-				(width 0.1)
+				(width 0.127)
 				(type solid)
 			)
@@
 		)
 		(pad "1" smd rect
-			(at -1.1 0.8)
-			(size 1.4 1.15)
+			(at -1.25 0)
+			(size 1.1 1.9)
 			(layers "F.Cu" "F.Mask" "F.Paste")
 			(net 41 "Net-(C83-Pad1)")
@@
 		)
 		(pad "2" smd rect
-			(at 1.1 0.8)
-			(size 1.4 1.15)
+			(at 1.25 0)
+			(size 1.1 1.9)
 			(layers "F.Cu" "F.Mask" "F.Paste")
 			(net 42 "Net-(C84-Pad1)")
@@
 			(solder_mask_margin 0.102)
 		)
-		(pad "3" smd rect
-			(at 1.1 -0.8)
-			(size 1.4 1.15)
-			(layers "F.Cu" "F.Mask" "F.Paste")
-			(solder_mask_margin 0.102)
-		)
-		(pad "4" smd rect
-			(at -1.1 -0.8)
-			(size 1.4 1.15)
-			(layers "F.Cu" "F.Mask" "F.Paste")
-			(solder_mask_margin 0.102)
-		)
 		(embedded_fonts no)
-		(model "${KIPRJMOD}/lib/3d_models/830100965009.stp"
+		(model "${KIPRJMOD}/lib/3d_models/ABS07-32.768KHZ-4-T--3DModel-STEP-400430.STEP"
 			(offset
 				(xyz 0 0 0)
@@
 			)
 			(rotate
-				(xyz 0 0 0)
+				(xyz -90 -0 -0)
 			)
 		)
